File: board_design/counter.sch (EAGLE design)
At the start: 24 parts, among them IC1 7805T

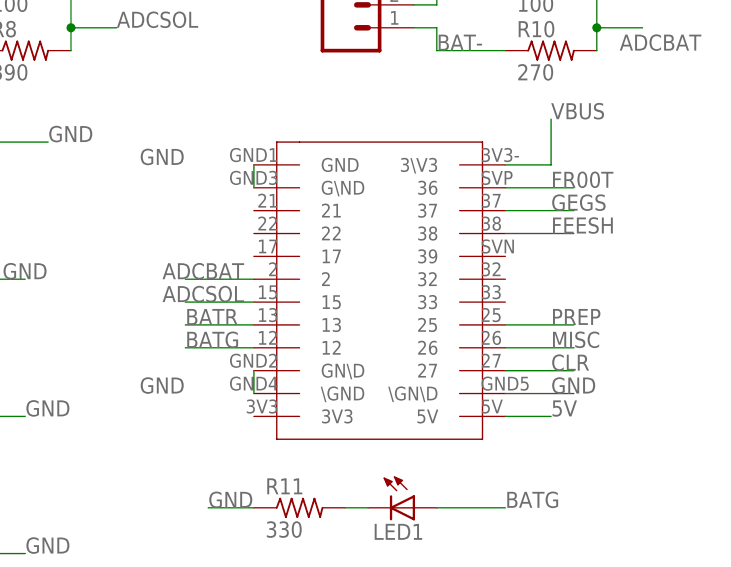
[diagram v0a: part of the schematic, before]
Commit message: Modified board not to have ADC on the boot pins (woops)
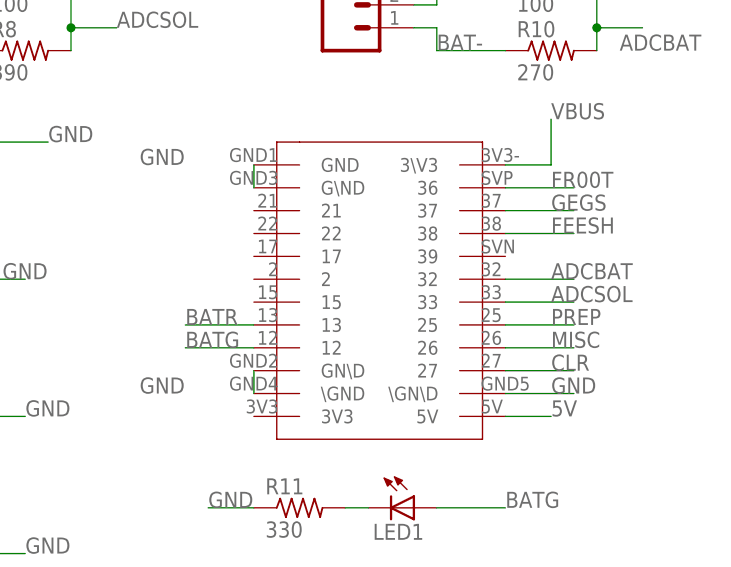
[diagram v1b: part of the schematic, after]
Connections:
- net ADCBAT: now also U$1.32; no longer U$1.2
- net ADCSOL: now also U$1.33; no longer U$1.15
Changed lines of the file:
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@@
 <net name="ADCSOL" class="0">
-<segment>
-<pinref part="U$1" gate="G$1" pin="15"/>
-<wire x1="66.04" y1="73.66" x2="58.42" y2="73.66" width="0.1524" layer="91"/>
-<label x="55.88" y="73.66" size="1.778" layer="95"/>
-</segment>
 <segment>
 <pinref part="R7" gate="G$1" pin="2"/>
@@
 <label x="50.8" y="104.14" size="1.778" layer="95"/>
 </segment>
+<segment>
+<pinref part="U$1" gate="G$1" pin="33"/>
+<wire x1="93.98" y1="73.66" x2="101.6" y2="73.66" width="0.1524" layer="91"/>
+<label x="99.06" y="73.66" size="1.778" layer="95"/>
+</segment>
 </net>
 <net name="ADCBAT" class="0">
-<segment>
-<pinref part="U$1" gate="G$1" pin="2"/>
-<wire x1="66.04" y1="76.2" x2="58.42" y2="76.2" width="0.1524" layer="91"/>
-<label x="55.88" y="76.2" size="1.778" layer="95"/>
-</segment>
 <segment>
 <pinref part="R9" gate="G$1" pin="2"/>
@@
 <label x="106.68" y="101.6" size="1.778" layer="95"/>
 </segment>
+<segment>
+<pinref part="U$1" gate="G$1" pin="32"/>
+<wire x1="93.98" y1="76.2" x2="101.6" y2="76.2" width="0.1524" layer="91"/>
+<label x="99.06" y="76.2" size="1.778" layer="95"/>
+</segment>
 </net>
